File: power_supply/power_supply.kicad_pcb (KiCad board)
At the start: 2 copper layers, 150 x 70 mm, 57 parts, among them J1 Conn_01x04_Male, J2 Conn_01x03_Male, J3 Conn_01x03_Male, J4 Conn_01x03_Male, J5 Conn_01x02_Male, J6 Conn_01x02_Male, U1 LM7815_TO220, U2 LM7915_TO220, U3 LM7815_TO220

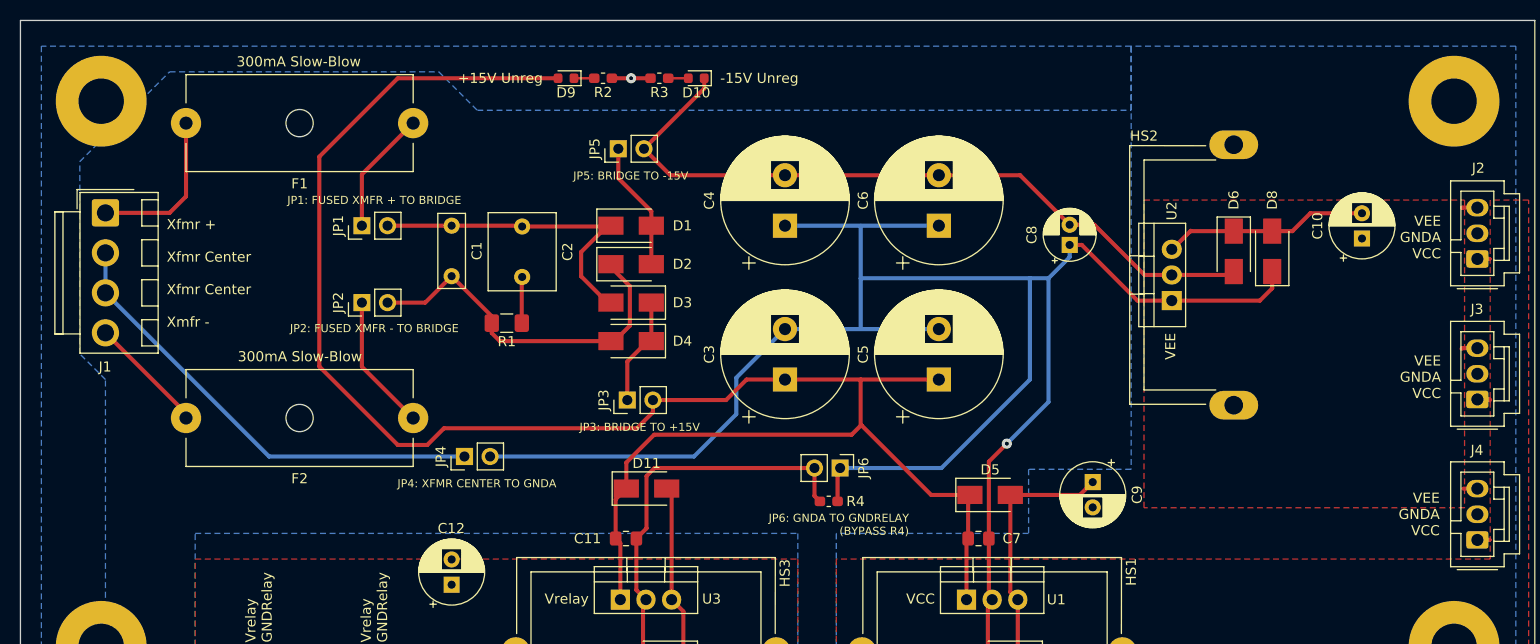
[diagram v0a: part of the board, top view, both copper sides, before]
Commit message: shrink layout for left side (up to reservoir caps)
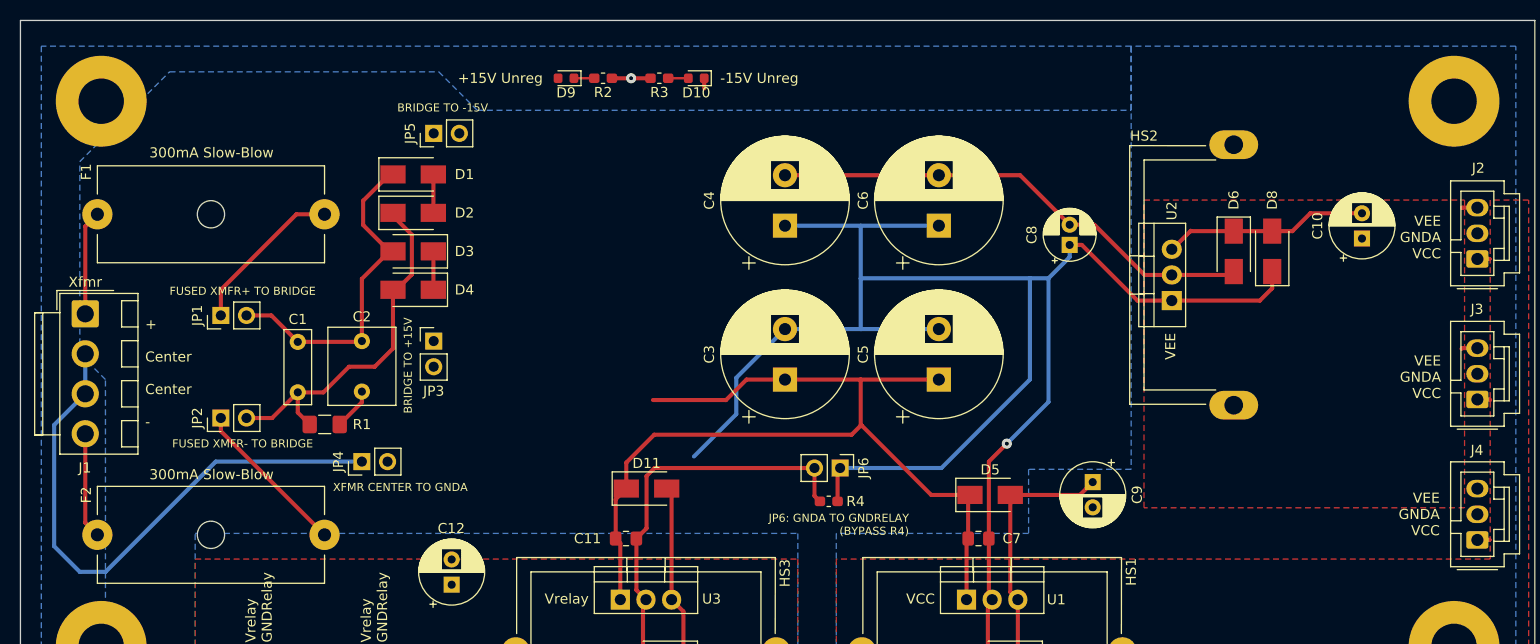
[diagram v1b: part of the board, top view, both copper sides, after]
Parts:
- R1: value 10-100 -> 100
- moved D1 22.2 mm to (88.9, 95.2)
- moved D2 22.2 mm to (88.9, 99.1)
- moved D3 22.2 mm to (88.9, 102.9)
- moved D4 22.2 mm to (88.9, 106.7)
- moved R1 20.6 mm to (80.1, 120.0)
- moved JP3 20.0 mm to (90.9, 111.8), turned to 0 degrees
- moved C2 19.5 mm to (83.8, 111.8)
- moved C1 19.1 mm to (77.5, 111.8)
- moved JP5 18.4 mm to (90.9, 91.2)
- moved JP2 18.1 mm to (69.8, 119.4)
- moved JP1 16.6 mm to (69.8, 109.2)
- moved F2 14.5 mm to (80.1, 130.9)
- moved F1 12.6 mm to (80.1, 99.2)
- moved J1 10.2 mm to (56.4, 109.1)
- moved JP4 10.2 mm to (83.8, 123.7)
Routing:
- net /+15_unreg: track 183.6 -> 97.2 mm
- net /-15_unreg: track 73.2 -> 49.7 mm
- net GNDA: track 205.8 -> 185.6 mm
- net /transformer_center: track 46.2 -> 56.4 mm
- net Net-(D1-Pad2): track 12.8 -> 3.81 mm
- net Net-(D3-Pad1): track 10.8 -> 3.81 mm
- net /transformer_plus: track 15.9 -> 10.4 mm
- net Net-(F1-Pad1): track 12.3 -> 15.9 mm
- net Net-(F2-Pad1): track 13.5 -> 15.8 mm
- net VEE: track 24.8 -> 23.5 mm
- net /transformer_minus: track 11.7 -> 10.5 mm
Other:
- board text added: "+ Center Center -"
- board text removed: "JP1: FUSED XMFR + TO BRIDGE"
- board text removed: "JP2: FUSED XMFR - TO BRIDGE"
- board text removed: "JP3: BRIDGE TO +15V"
- board text removed: "JP4: XFMR CENTER TO GNDA"
- board text removed: "JP5: BRIDGE TO -15V"
- board text removed: "Xfmr + Xfmr Center Xfmr Center Xmfr -"

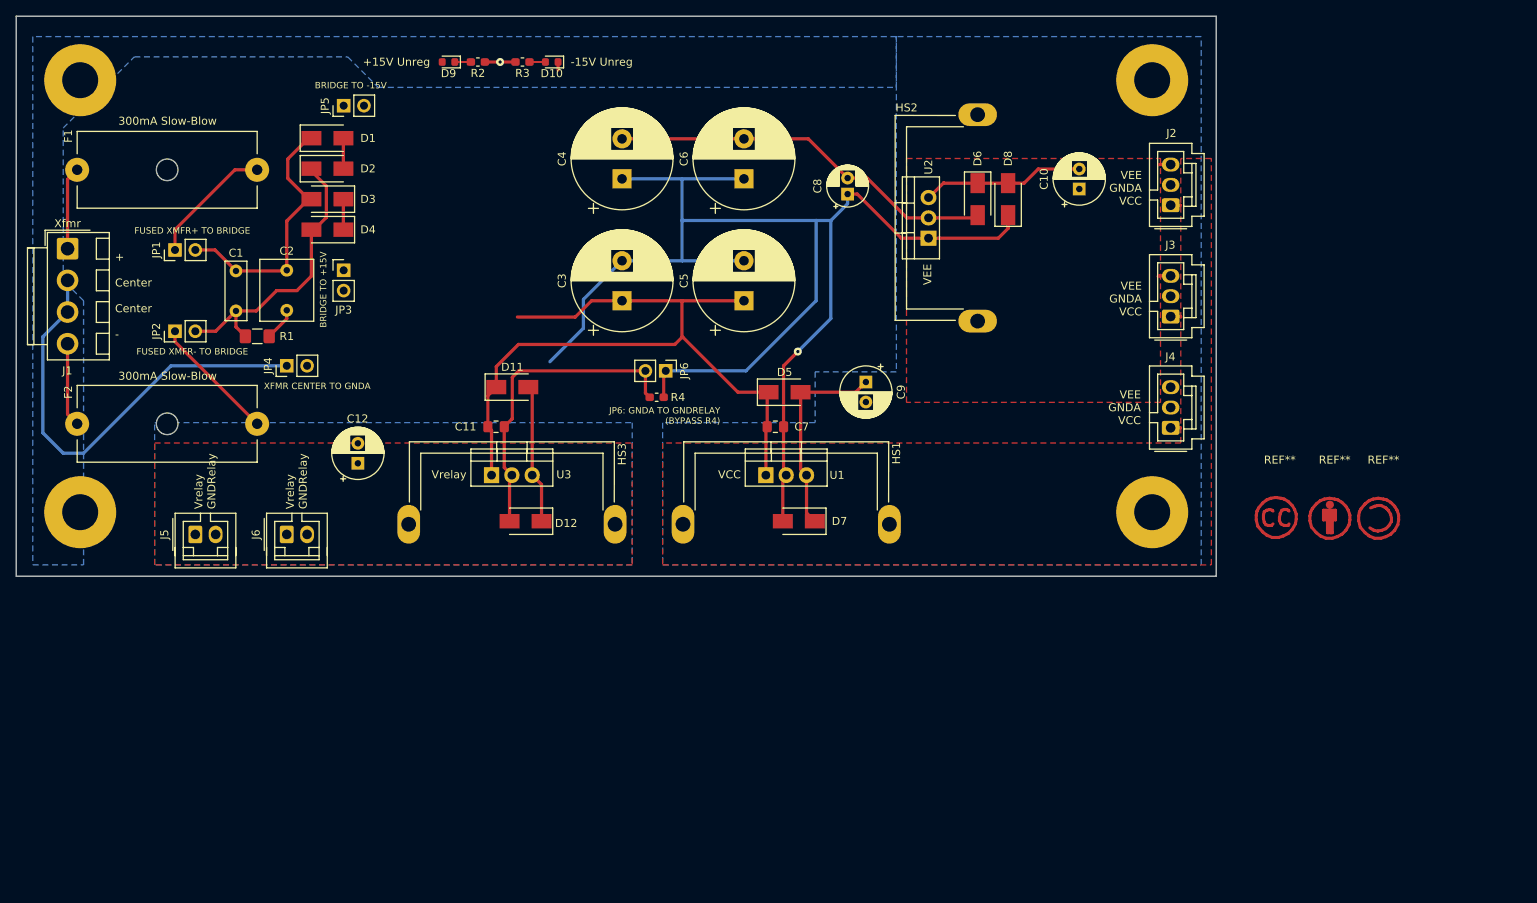
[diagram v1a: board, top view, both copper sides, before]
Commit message: change floating PCB text to footprint text
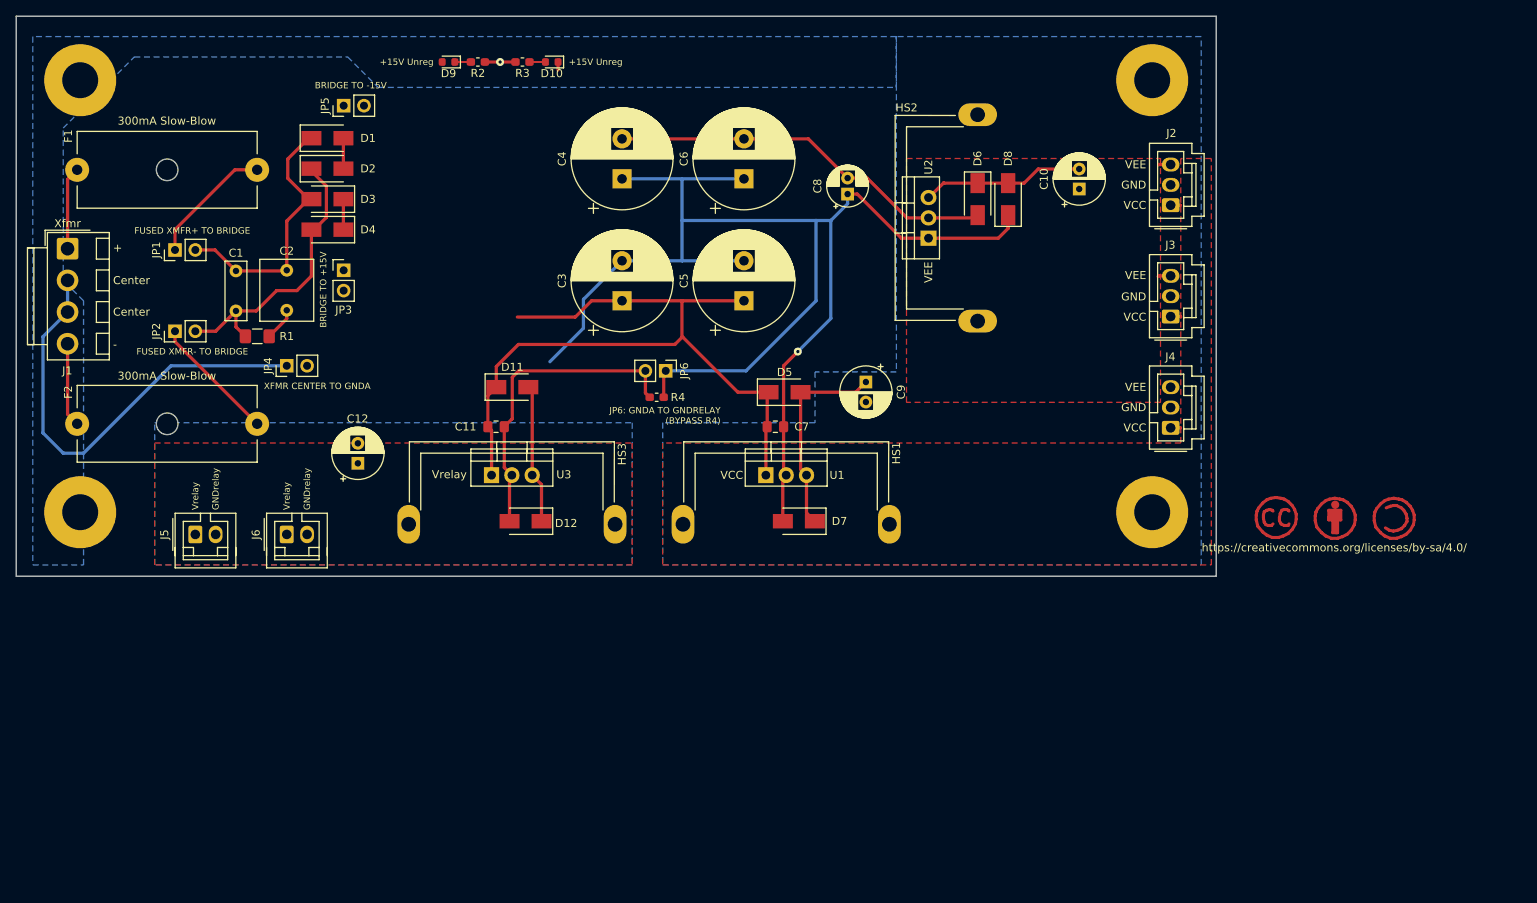
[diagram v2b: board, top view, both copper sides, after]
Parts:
- moved REF** 1.94 mm to (222.2, 142.8)
- moved REF** 0.67 mm to (214.9, 142.8)
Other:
- board text removed: "+ Center Center -"
- board text removed: "+15V Unreg"
- board text removed: "-15V Unreg"
- board text removed: "300mA Slow-Blow"
- board text removed: "JP6: GNDA TO GNDRELAY (BYPASS R4)"
- board text removed: "VCC"
- board text removed: "VEE"
- board text removed: "VEE GNDA VCC"
- board text removed: "Vrelay"
- board text removed: "Vrelay GNDRelay"

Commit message: move graphic symbols off-board temporarily and update TODO
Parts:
- moved REF** 46.1 mm to (216.0, 120.5)
- moved REF** 41.2 mm to (222.5, 133.1)
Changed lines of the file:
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@@
   )
   (module Symbol:OSHW-Logo2_9.8x8mm_SilkScreen locked (layer B.Cu)
-    (at 181.318 131.204 180)
+    (at 222.504 133.096 180)
     (descr "Open Source Hardware Symbol")
     (tags "Logo Symbol OSHW")
@@
   )
   (module Symbol:KiCad-Logo2_8mm_SilkScreen locked (layer B.Cu)
-    (at 174.841 141.237 180)
+    (at 216.027 120.523 180)
     (descr "KiCad Logo")
     (tags "Logo KiCad")
@@
     (arrow2b (pts (xy 58 157.479999) (xy 59.126504 156.893578)))
   )
-  (gr_text "TODO\nfix C9, C10\nadd planes\nmake smaller" (at 163.83 140.97) (layer Cmts.User)
+  (gr_text "TODO\nfix C9, C10\nadd planes\nmake smaller" (at 204.47 133.35) (layer Cmts.User)
     (effects (font (size 1 1) (thickness 0.15)) (justify left))
   )

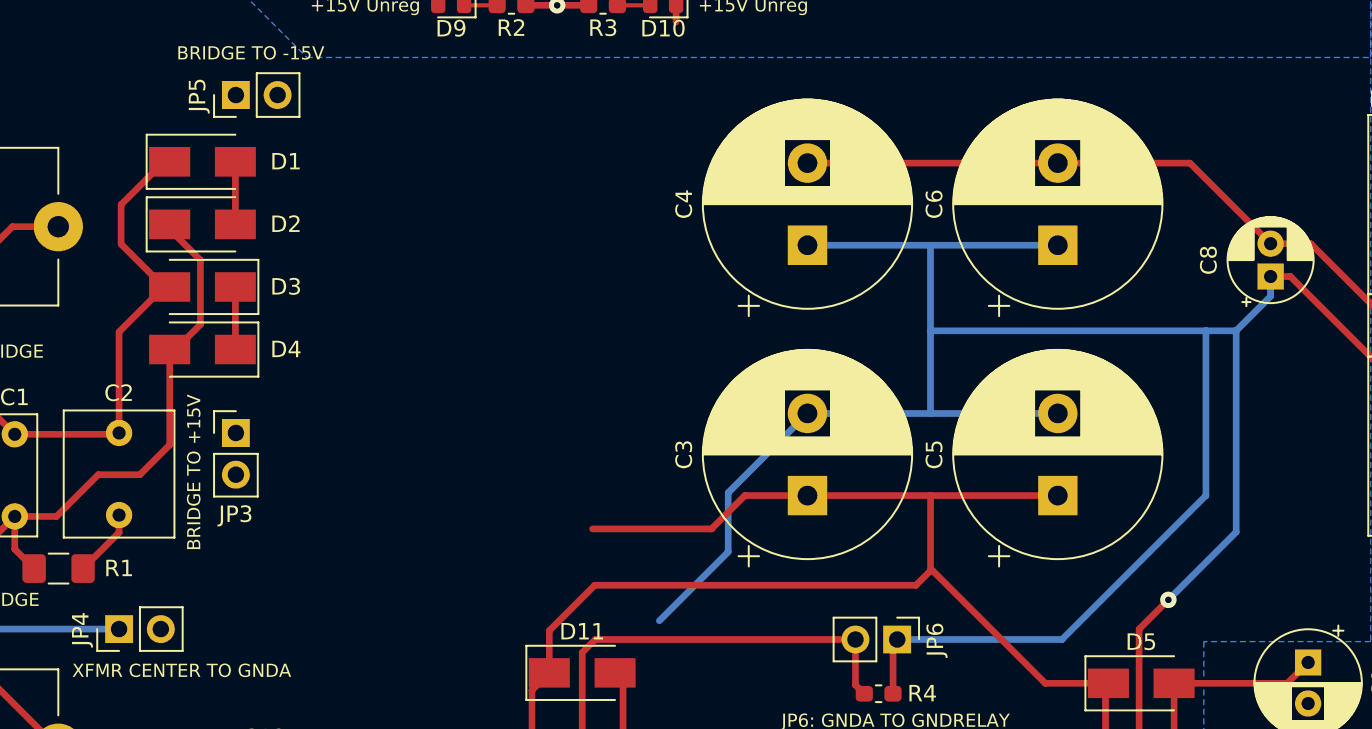
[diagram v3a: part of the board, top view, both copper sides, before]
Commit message: remove extra reservoir caps from layout and move remaining once to new location
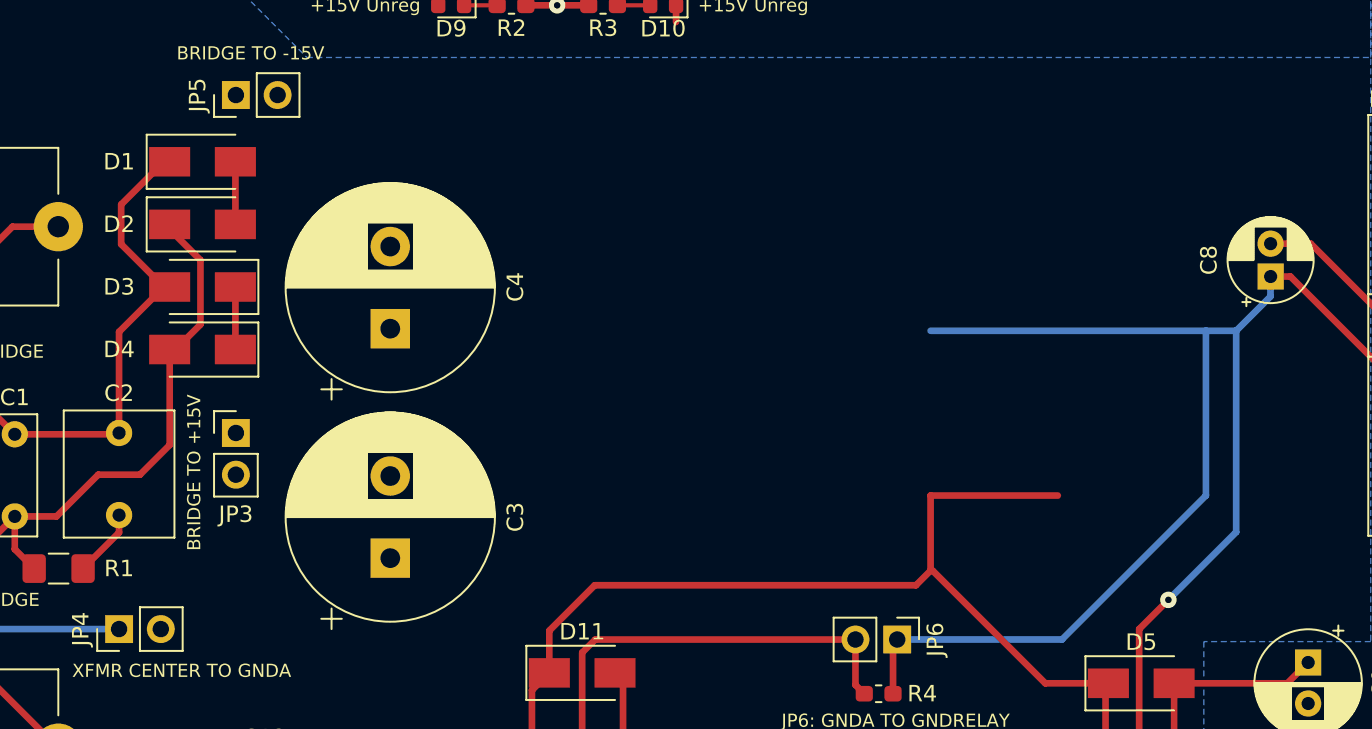
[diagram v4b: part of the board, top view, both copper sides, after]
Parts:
- removed C5, C6: 1000u, Capacitor_THT:CP_Radial_D12.5mm_P5.00mm
- moved C4 25.9 mm to (100.3, 105.4)
- moved C3 25.7 mm to (100.3, 119.4)
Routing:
- net GNDA: track 185.6 -> 128.5 mm
- net /-15_unreg: track 49.7 -> 19.5 mm
- net /+15_unreg: track 97.2 -> 75.8 mm
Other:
- board text added: "TODO fix C9, C10 add planes make smaller check to-220 dimensions for actual 7815 used"
- board text removed: "TODO fix C9, C10 add planes make smaller"
